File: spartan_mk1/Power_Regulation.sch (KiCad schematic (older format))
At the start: 30 parts, among them J14 Conn_01x02_Female, Q3 AO3401A, U5 NCP1117-3.3_TO252, U6 TPS5430DDA

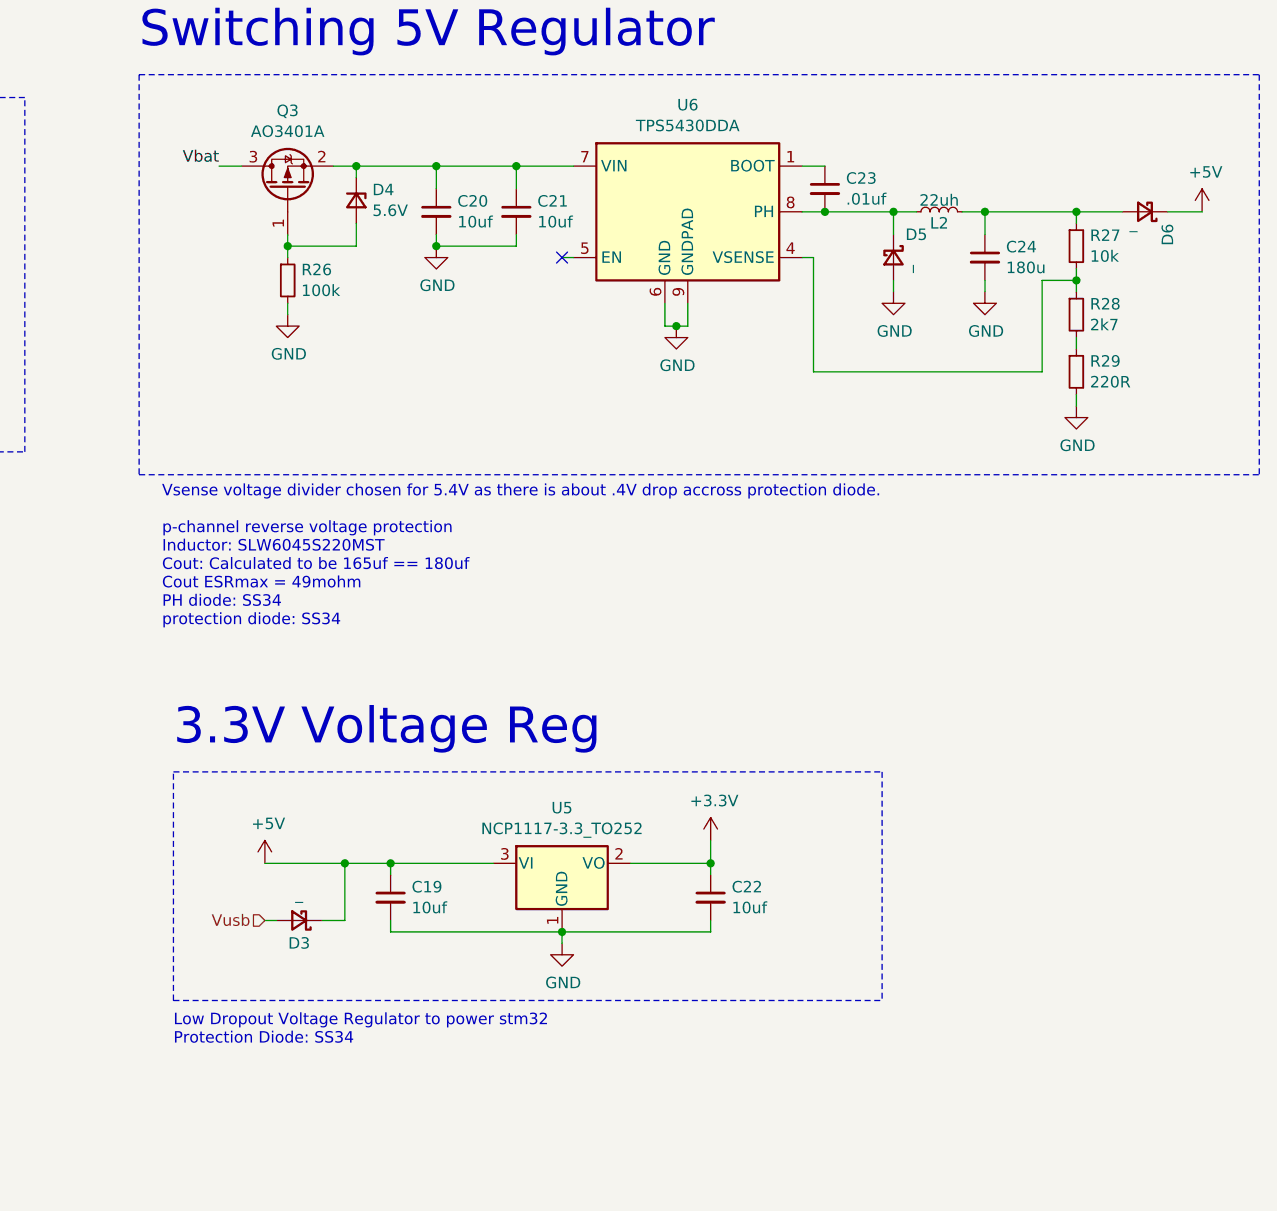
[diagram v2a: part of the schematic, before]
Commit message: Almost complete PCB layout (no routing)
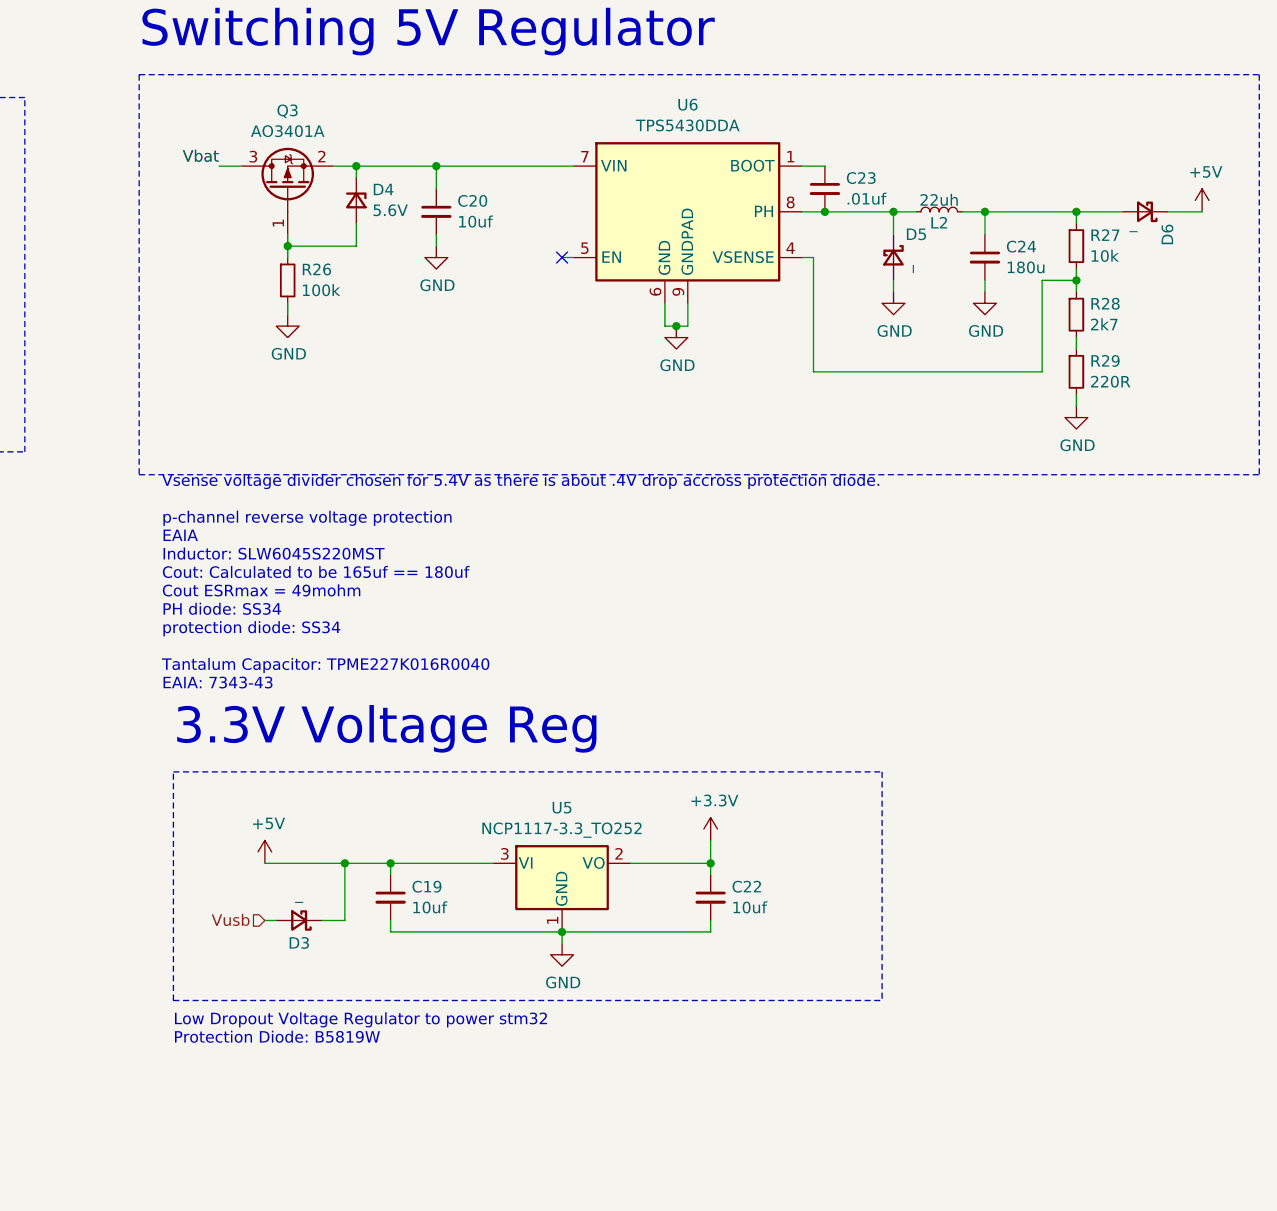
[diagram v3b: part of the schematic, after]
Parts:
- removed C21: 10uf, Capacitor_SMD:C_1206_3216Metric, symbol Device:C_Small
- C24: footprint Capacitor_SMD:C_0805_2012Metric_Pad1.15x1.40mm_HandSolder -> Capacitor_Tantalum_SMD:CP_EIA-7343-43_Kemet-X_Pad2.25x2.55mm_HandSolder
- D3: footprint Diode_SMD:D_SMA -> Diode_SMD:D_SOD-123
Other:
- note added: "Low Dropout Voltage Regulator to power stm32\nProtection Diode: B5819W"
- note added: "Vsense voltage divider chosen for 5.4V as there is about .4V drop accross protection diode.\n\np-channel reverse voltage protection\nEAIA\nInductor: SLW6045S220MST\nCout: Calculated to be 165uf == 180uf\nCout ESRmax = 49mohm\nPH diode: SS34\nprotection diode: SS34\n\nTantalum Capacitor: TPME227K016R0040\nEAIA: 7343-43"
- note removed: "Low Dropout Voltage Regulator to power stm32\nProtection Diode: SS34"
- note removed: "Vsense voltage divider chosen for 5.4V as there is about .4V drop accross protection diode.\n\np-channel reverse voltage protection\nInductor: SLW6045S220MST\nCout: Calculated to be 165uf == 180uf\nCout ESRmax = 49mohm\nPH diode: SS34\nprotection diode: SS34\n\n"
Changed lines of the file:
@@
 	6150 5000 6150 4000
 Text Notes 6150 5200 0    50   ~ 0
-Low Dropout Voltage Regulator to power stm32\nProtection Diode: SS34
+Low Dropout Voltage Regulator to power stm32\nProtection Diode: B5819W
 $Comp
 L Regulator_Linear:NCP1117-3.3_TO252 U?
@@
 	7300 1700 7300 1650
 Wire Wire Line
-	7300 1350 7650 1350
-Wire Wire Line
 	7850 1750 7900 1750
 $Comp
@@
 F 0 "C24" H 9792 1796 50  0000 L CNN
 F 1 "180u" H 9792 1705 50  0000 L CNN
-F 2 "Capacitor_SMD:C_0805_2012Metric_Pad1.15x1.40mm_HandSolder" H 9700 1750 50  0001 C CNN
+F 2 "Capacitor_Tantalum_SMD:CP_EIA-7343-43_Kemet-X_Pad2.25x2.55mm_HandSolder" H 9700 1750 50  0001 C CNN
 F 3 "~" H 9700 1750 50  0001 C CNN
 	1    9700 1750
@@
 Connection ~ 8350 2050
 NoConn ~ 7850 1750
-$Comp
-L Device:C_Small C?
-U 1 1 5F88DC45
-P 7650 1550
-AR Path="/5F78701C/5F88DC45" Ref="C?"  Part="1"
-AR Path="/5F79A745/5F88DC45" Ref="C21"  Part="1"
-F 0 "C21" H 7742 1596 50  0000 L CNN
-F 1 "10uf" H 7742 1505 50  0000 L CNN
-F 2 "Capacitor_SMD:C_1206_3216Metric" H 7650 1550 50  0001 C CNN
-F 3 "~" H 7650 1550 50  0001 C CNN
-	1    7650 1550
-	1    0    0    -1
-$EndComp
-Wire Wire Line
-	7650 1450 7650 1350
-Connection ~ 7650 1350
-Wire Wire Line
-	7650 1350 7900 1350
-Wire Wire Line
-	7650 1650 7650 1700
-Wire Wire Line
-	7650 1700 7300 1700
-Connection ~ 7300 1700
-Text Notes 6100 3450 0    50   ~ 0
-Vsense voltage divider chosen for 5.4V as there is about .4V drop accross protection diode.\n\np-channel reverse voltage protection\nInductor: SLW6045S220MST\nCout: Calculated to be 165uf == 180uf\nCout ESRmax = 49mohm\nPH diode: SS34\nprotection diode: SS34\n\n
+Text Notes 6100 3650 0    50   ~ 0
+Vsense voltage divider chosen for 5.4V as there is about .4V drop accross protection diode.\n\np-channel reverse voltage protection\nEAIA\nInductor: SLW6045S220MST\nCout: Calculated to be 165uf == 180uf\nCout ESRmax = 49mohm\nPH diode: SS34\nprotection diode: SS34\n\nTantalum Capacitor: TPME227K016R0040\nEAIA: 7343-43
 $Comp
 L Device:R_Small R28
@@
 F 0 "D3" H 6700 4750 50  0000 C CNN
 F 1 "_" H 6700 4534 50  0000 C CNN
-F 2 "Diode_SMD:D_SMA" V 6700 4650 50  0001 C CNN
+F 2 "Diode_SMD:D_SOD-123" V 6700 4650 50  0001 C CNN
 F 3 "~" V 6700 4650 50  0001 C CNN
 	1    6700 4650
@@
 	1950 4200 1950 4150
 Connection ~ 1950 4150
+Wire Wire Line
+	7300 1350 7900 1350
 $EndSCHEMATC

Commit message: updated placement
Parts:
- removed U5: NCP1117-3.3_TO252, Package_TO_SOT_SMD:TO-252-2, symbol Regulator_Linear:NCP1117-3.3_TO252
- added U?: AMS1117-3.3, Package_TO_SOT_SMD:SOT-223-3_TabPin2, symbol Regulator_Linear:AMS1117-3.3
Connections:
- net +3V3: now also U?.2 (VO)
- net +5V: now also U?.3 (VI)
- net GND: now also U?.1 (GND)
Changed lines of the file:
@@
 Low Dropout Voltage Regulator to power stm32\nProtection Diode: B5819W
-$Comp
-L Regulator_Linear:NCP1117-3.3_TO252 U?
-U 1 1 5F7A601F
-P 7850 4400
-AR Path="/5F78701C/5F7A601F" Ref="U?"  Part="1"
-AR Path="/5F79A745/5F7A601F" Ref="U5"  Part="1"
-F 0 "U5" H 7850 4642 50  0000 C CNN
-F 1 "NCP1117-3.3_TO252" H 7850 4551 50  0000 C CNN
-F 2 "Package_TO_SOT_SMD:TO-252-2" H 7850 4625 50  0001 C CNN
-F 3 "http://www.onsemi.com/pub_link/Collateral/NCP1117-D.PDF" H 7850 4400 50  0001 C CNN
-	1    7850 4400
-	1    0    0    -1
-$EndComp
 $Comp
 L Device:LED_Small D?
@@
 Wire Wire Line
 	7300 1350 7900 1350
+$Comp
+L Regulator_Linear:AMS1117-3.3 U?
+U 1 1 5FA17F2E
+P 7850 4400
+F 0 "U?" H 7850 4642 50  0000 C CNN
+F 1 "AMS1117-3.3" H 7850 4551 50  0000 C CNN
+F 2 "Package_TO_SOT_SMD:SOT-223-3_TabPin2" H 7850 4600 50  0001 C CNN
+F 3 "http://www.advanced-monolithic.com/pdf/ds1117.pdf" H 7950 4150 50  0001 C CNN
+	1    7850 4400
+	1    0    0    -1
+$EndComp
 $EndSCHEMATC

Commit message: Routing in progress
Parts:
- gave numbers to parts that had none: 1
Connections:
- net Vbat: no longer C18.1, R22.2
- new net ESC_BAT_SENSE: C18.1, R22.2
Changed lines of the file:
@@
 $Descr A4 11693 8268
 encoding utf-8
-Sheet 5 6
+Sheet 3 6
 Title ""
 Date ""
@@
 Wire Wire Line
 	2200 3750 1950 3750
-Connection ~ 1950 3750
 Wire Wire Line
 	1950 3750 1950 3850
@@
 	1    0    0    -1
 $EndComp
-Text Label 1400 3750 2    50   ~ 0
-Vbat
 Text Notes 1050 3500 0    157  ~ 0
 Battery Voltage Sensing
@@
 	950  7200 950  5900
 Wire Wire Line
-	1400 3750 1950 3750
-Wire Wire Line
 	1950 4200 1950 4150
 Connection ~ 1950 4150
@@
 	7300 1350 7900 1350
 $Comp
-L Regulator_Linear:AMS1117-3.3 U?
+L Regulator_Linear:AMS1117-3.3 U5
 U 1 1 5FA17F2E
 P 7850 4400
-F 0 "U?" H 7850 4642 50  0000 C CNN
+F 0 "U5" H 7850 4642 50  0000 C CNN
 F 1 "AMS1117-3.3" H 7850 4551 50  0000 C CNN
 F 2 "Package_TO_SOT_SMD:SOT-223-3_TabPin2" H 7850 4600 50  0001 C CNN
@@
 	1    0    0    -1
 $EndComp
+Text HLabel 1850 3750 0    50   Input ~ 0
+ESC_BAT_SENSE
+Wire Wire Line
+	1850 3750 1950 3750
+Connection ~ 1950 3750
 $EndSCHEMATC

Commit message: Generated gerber files. Positions and BOM assemly files generated
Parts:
- C18: LCSC (none) -> C57112; LCSC Part # (none) -> C57112
- C19: LCSC (none) -> C15850; LCSC Part # (none) -> C15850
- C20: LCSC (none) -> C13585; LCSC Part # (none) -> C13585
- C22: LCSC (none) -> C19702; LCSC Part # (none) -> C19702
- C23: LCSC (none) -> C15195; LCSC Part # (none) -> C15195
- C24: footprint Capacitor_Tantalum_SMD:CP_EIA-7343-43_Kemet-X_Pad2.25x2.55mm_HandSolder -> Capacitor_Tantalum_SMD:CP_EIA-7343-43
- D1, D2: value LED_Small -> LED_RED; LCSC (none) -> C2286; LCSC Part # (none) -> C2286
- D3: LCSC (none) -> C8598; LCSC Part # (none) -> C8598
- D4: LCSC (none) -> C8062; LCSC Part # (none) -> C8062
- D5, D6: LCSC (none) -> C8678; LCSC Part # (none) -> C8678
- L2: LCSC (none) -> C206321; LCSC Part # (none) -> C206321
- Q3: LCSC (none) -> C15127; LCSC Part # (none) -> C15127
- R22: LCSC (none) -> C23024; LCSC Part # (none) -> C23024
- R23: LCSC (none) -> C23172; LCSC Part # (none) -> C23172
- R24, R25: LCSC (none) -> C25900; LCSC Part # (none) -> C25900
- R26: LCSC (none) -> C17407; LCSC Part # (none) -> C17407
- R27: LCSC (none) -> C25744; LCSC Part # (none) -> C25744
- R28: value 2k7 -> 2k2; LCSC (none) -> C25879; LCSC Part # (none) -> C25879
- R29: value 220R -> 680R; LCSC (none) -> C25130; LCSC Part # (none) -> C25130
- U5: LCSC (none) -> C6186; LCSC Part # (none) -> C6186
- U6: LCSC (none) -> C9864; LCSC Part # (none) -> C9864
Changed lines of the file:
@@
 F 2 "Capacitor_SMD:C_0805_2012Metric" H 7100 4550 50  0001 C CNN
 F 3 "~" H 7100 4550 50  0001 C CNN
+F 4 "C15850" H 7100 4550 50  0001 C CNN "LCSC Part #"
+F 5 "C15850" H 7100 4550 50  0001 C CNN "LCSC"
 	1    7100 4550
 	1    0    0    -1
@@
 F 2 "Capacitor_SMD:C_0603_1608Metric" H 8500 4550 50  0001 C CNN
 F 3 "~" H 8500 4550 50  0001 C CNN
+F 4 "C19702" H 8500 4550 50  0001 C CNN "LCSC Part #"
+F 5 "C19702" H 8500 4550 50  0001 C CNN "LCSC"
 	1    8500 4550
 	1    0    0    -1
@@
 AR Path="/5F79A745/5F7A6056" Ref="D2"  Part="1"
 F 0 "D2" V 4996 1530 50  0000 R CNN
-F 1 "LED_Small" V 4905 1530 50  0000 R CNN
+F 1 "LED_RED" V 4905 1530 50  0000 R CNN
 F 2 "LED_SMD:LED_0603_1608Metric" V 4950 1600 50  0001 C CNN
 F 3 "~" V 4950 1600 50  0001 C CNN
+F 4 "C2286" H 4950 1600 50  0001 C CNN "LCSC Part #"
+F 5 "C2286" H 4950 1600 50  0001 C CNN "LCSC"
 	1    4950 1600
 	0    -1   -1   0
@@
 F 2 "Resistor_SMD:R_0402_1005Metric" H 4950 1850 50  0001 C CNN
 F 3 "~" H 4950 1850 50  0001 C CNN
+F 4 "C25900" H 4950 1850 50  0001 C CNN "LCSC Part #"
+F 5 "C25900" H 4950 1850 50  0001 C CNN "LCSC"
 	1    4950 1850
 	1    0    0    -1
@@
 F 2 "Package_SO:TI_SO-PowerPAD-8_ThermalVias" H 8450 1200 50  0001 L CIN
 F 3 "http://www.ti.com/lit/ds/symlink/tps5430.pdf" H 8400 1550 50  0001 C CNN
+F 4 "C9864" H 8400 1550 50  0001 C CNN "LCSC Part #"
+F 5 "C9864" H 8400 1550 50  0001 C CNN "LCSC"
 	1    8400 1550
 	1    0    0    -1
@@
 F 2 "Capacitor_SMD:C_1206_3216Metric" H 7300 1550 50  0001 C CNN
 F 3 "~" H 7300 1550 50  0001 C CNN
+F 4 "C13585" H 7300 1550 50  0001 C CNN "LCSC Part #"
+F 5 "C13585" H 7300 1550 50  0001 C CNN "LCSC"
 	1    7300 1550
 	1    0    0    -1
@@
 F 2 "Capacitor_SMD:C_0402_1005Metric" H 9000 1450 50  0001 C CNN
 F 3 "~" H 9000 1450 50  0001 C CNN
+F 4 "C15195" H 9000 1450 50  0001 C CNN "LCSC Part #"
+F 5 "C15195" H 9000 1450 50  0001 C CNN "LCSC"
 	1    9000 1450
 	1    0    0    -1
@@
 F 2 "Diode_SMD:D_SMA" V 9300 1750 50  0001 C CNN
 F 3 "~" V 9300 1750 50  0001 C CNN
+F 4 "C8678" H 9300 1750 50  0001 C CNN "LCSC Part #"
+F 5 "C8678" H 9300 1750 50  0001 C CNN "LCSC"
 	1    9300 1750
 	0    1    1    0
@@
 F 2 "Inductor_SMD:SLW6045_6mmX6mm" H 9500 1550 50  0001 C CNN
 F 3 "~" H 9500 1550 50  0001 C CNN
+F 4 "C206321" H 9500 1550 50  0001 C CNN "LCSC Part #"
+F 5 "C206321" H 9500 1550 50  0001 C CNN "LCSC"
 	1    9500 1550
 	0    -1   -1   0
@@
 F 0 "C24" H 9792 1796 50  0000 L CNN
 F 1 "180u" H 9792 1705 50  0000 L CNN
-F 2 "Capacitor_Tantalum_SMD:CP_EIA-7343-43_Kemet-X_Pad2.25x2.55mm_HandSolder" H 9700 1750 50  0001 C CNN
+F 2 "Capacitor_Tantalum_SMD:CP_EIA-7343-43" H 9700 1750 50  0001 C CNN
 F 3 "~" H 9700 1750 50  0001 C CNN
 	1    9700 1750
@@
 P 10100 2000
 F 0 "R28" H 10159 2046 50  0000 L CNN
-F 1 "2k7" H 10159 1955 50  0000 L CNN
+F 1 "2k2" H 10159 1955 50  0000 L CNN
 F 2 "Resistor_SMD:R_0402_1005Metric" H 10100 2000 50  0001 C CNN
 F 3 "~" H 10100 2000 50  0001 C CNN
+F 4 "C25879" H 10100 2000 50  0001 C CNN "LCSC Part #"
+F 5 "C25879" H 10100 2000 50  0001 C CNN "LCSC"
 	1    10100 2000
 	1    0    0    -1
@@
 P 10100 2250
 F 0 "R29" H 10159 2296 50  0000 L CNN
-F 1 "220R" H 10159 2205 50  0000 L CNN
+F 1 "680R" H 10159 2205 50  0000 L CNN
 F 2 "Resistor_SMD:R_0402_1005Metric" H 10100 2250 50  0001 C CNN
 F 3 "~" H 10100 2250 50  0001 C CNN
+F 4 "C25130" H 10100 2250 50  0001 C CNN "LCSC Part #"
+F 5 "C25130" H 10100 2250 50  0001 C CNN "LCSC"
 	1    10100 2250
 	1    0    0    -1
@@
 AR Path="/5F79A745/5F8C82A6" Ref="D1"  Part="1"
 F 0 "D1" V 4046 1530 50  0000 R CNN
-F 1 "LED_Small" V 3955 1530 50  0000 R CNN
+F 1 "LED_RED" V 3955 1530 50  0000 R CNN
 F 2 "LED_SMD:LED_0603_1608Metric" V 4000 1600 50  0001 C CNN
 F 3 "~" V 4000 1600 50  0001 C CNN
+F 4 "C2286" H 4000 1600 50  0001 C CNN "LCSC Part #"
+F 5 "C2286" H 4000 1600 50  0001 C CNN "LCSC"
 	1    4000 1600
 	0    -1   -1   0
@@
 F 2 "Resistor_SMD:R_0402_1005Metric" H 4000 1850 50  0001 C CNN
 F 3 "~" H 4000 1850 50  0001 C CNN
+F 4 "C25900" H 4000 1850 50  0001 C CNN "LCSC Part #"
+F 5 "C25900" H 4000 1850 50  0001 C CNN "LCSC"
 	1    4000 1850
 	1    0    0    -1
@@
 F 2 "Resistor_SMD:R_0402_1005Metric" H 10100 1700 50  0001 C CNN
 F 3 "~" H 10100 1700 50  0001 C CNN
+F 4 "C25744" H 10100 1700 50  0001 C CNN "LCSC Part #"
+F 5 "C25744" H 10100 1700 50  0001 C CNN "LCSC"
 	1    10100 1700
 	1    0    0    -1
@@
 F 2 "Diode_SMD:D_SOD-123" V 6700 4650 50  0001 C CNN
 F 3 "~" V 6700 4650 50  0001 C CNN
+F 4 "C8598" H 6700 4650 50  0001 C CNN "LCSC Part #"
+F 5 "C8598" H 6700 4650 50  0001 C CNN "LCSC"
 	1    6700 4650
 	-1   0    0    1
@@
 F 2 "Package_TO_SOT_SMD:SOT-23" H 6850 1375 50  0001 L CIN
 F 3 "http://www.aosmd.com/pdfs/datasheet/AO3401A.pdf" H 6650 1450 50  0001 L CNN
+F 4 "C15127" H 6650 1450 50  0001 C CNN "LCSC Part #"
+F 5 "C15127" H 6650 1450 50  0001 C CNN "LCSC"
 	1    6650 1450
 	0    -1   -1   0
@@
 F 2 "Diode_SMD:D_MiniMELF" V 6950 1500 50  0001 C CNN
 F 3 "~" V 6950 1500 50  0001 C CNN
+F 4 "C8062" H 6950 1500 50  0001 C CNN "LCSC Part #"
+F 5 "C8062" H 6950 1500 50  0001 C CNN "LCSC"
 	1    6950 1500
 	0    1    1    0
@@
 F 2 "Resistor_SMD:R_0805_2012Metric" H 6650 1850 50  0001 C CNN
 F 3 "~" H 6650 1850 50  0001 C CNN
+F 4 "C17407" H 6650 1850 50  0001 C CNN "LCSC Part #"
+F 5 "C17407" H 6650 1850 50  0001 C CNN "LCSC"
 	1    6650 1850
 	1    0    0    -1
@@
 F 2 "Diode_SMD:D_SMA" V 10400 1550 50  0001 C CNN
 F 3 "~" V 10400 1550 50  0001 C CNN
+F 4 "C8678" H 10400 1550 50  0001 C CNN "LCSC Part #"
+F 5 "C8678" H 10400 1550 50  0001 C CNN "LCSC"
 	1    10400 1550
 	-1   0    0    1
@@
 F 2 "Resistor_SMD:R_0603_1608Metric" H 2700 3950 50  0001 C CNN
 F 3 "~" H 2700 3950 50  0001 C CNN
+F 4 "C23172" H 2700 3950 50  0001 C CNN "LCSC Part #"
+F 5 "C23172" H 2700 3950 50  0001 C CNN "LCSC"
 	1    2700 3950
 	-1   0    0    1
@@
 F 2 "Resistor_SMD:R_0603_1608Metric" H 2300 3750 50  0001 C CNN
 F 3 "~" H 2300 3750 50  0001 C CNN
+F 4 "C23024" H 2300 3750 50  0001 C CNN "LCSC Part #"
+F 5 "C23024" H 2300 3750 50  0001 C CNN "LCSC"
 	1    2300 3750
 	0    1    1    0
@@
 F 2 "Capacitor_SMD:C_0603_1608Metric" H 1950 3950 50  0001 C CNN
 F 3 "~" H 1950 3950 50  0001 C CNN
+F 4 "C57112" H 1950 3950 50  0001 C CNN "LCSC Part #"
+F 5 "C57112" H 1950 3950 50  0001 C CNN "LCSC"
 	1    1950 3950
 	1    0    0    -1
@@
 F 2 "Package_TO_SOT_SMD:SOT-223-3_TabPin2" H 7850 4600 50  0001 C CNN
 F 3 "http://www.advanced-monolithic.com/pdf/ds1117.pdf" H 7950 4150 50  0001 C CNN
+F 4 "C6186" H 7850 4400 50  0001 C CNN "LCSC Part #"
+F 5 "C6186" H 7850 4400 50  0001 C CNN "LCSC"
 	1    7850 4400
 	1    0    0    -1
